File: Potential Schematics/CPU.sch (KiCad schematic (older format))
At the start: 0 parts

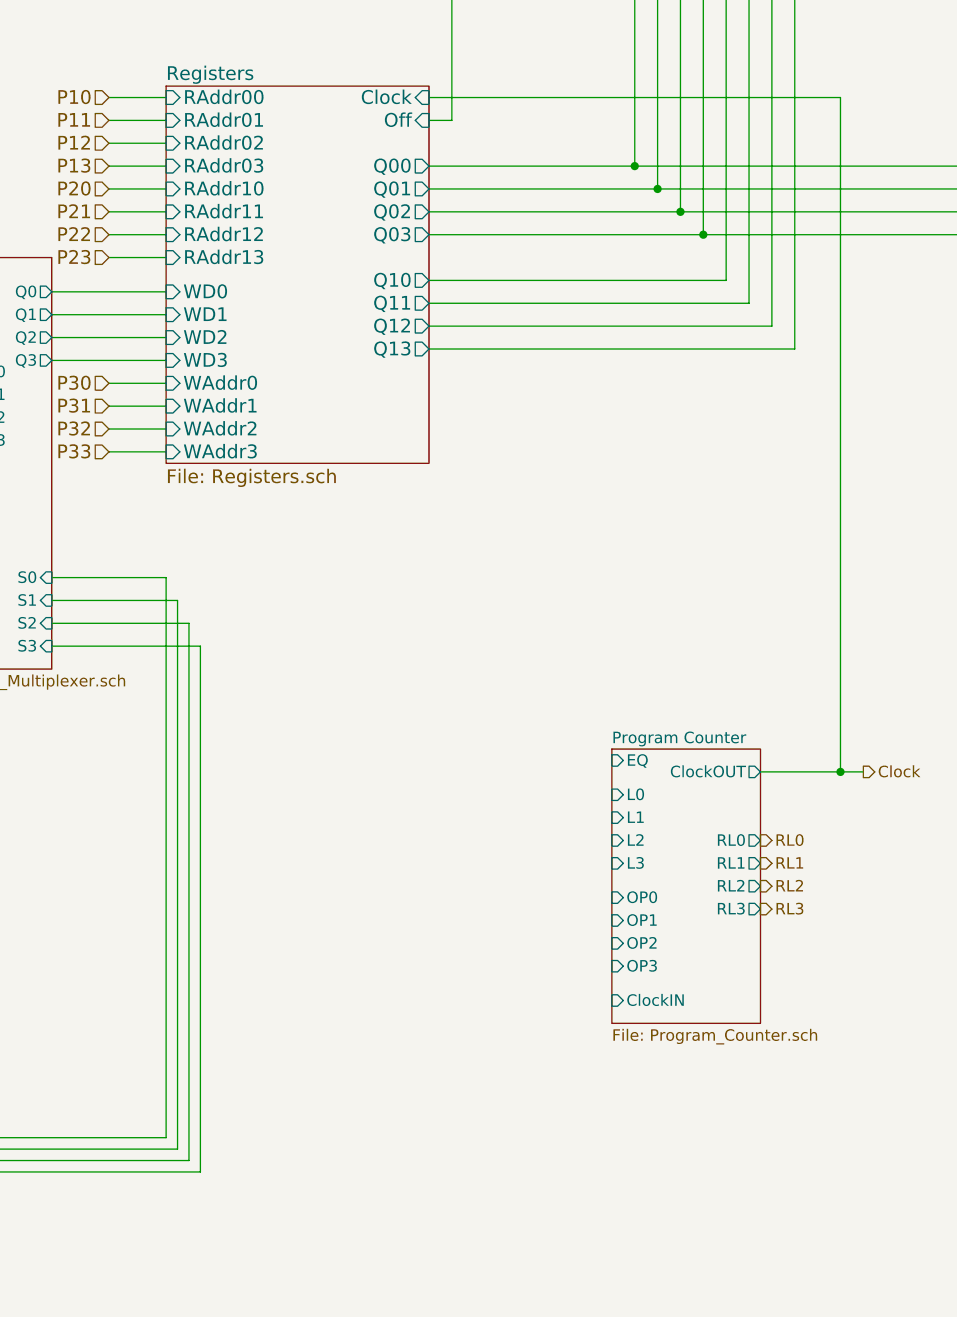
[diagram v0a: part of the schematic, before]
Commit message: In the middle of adding ROM
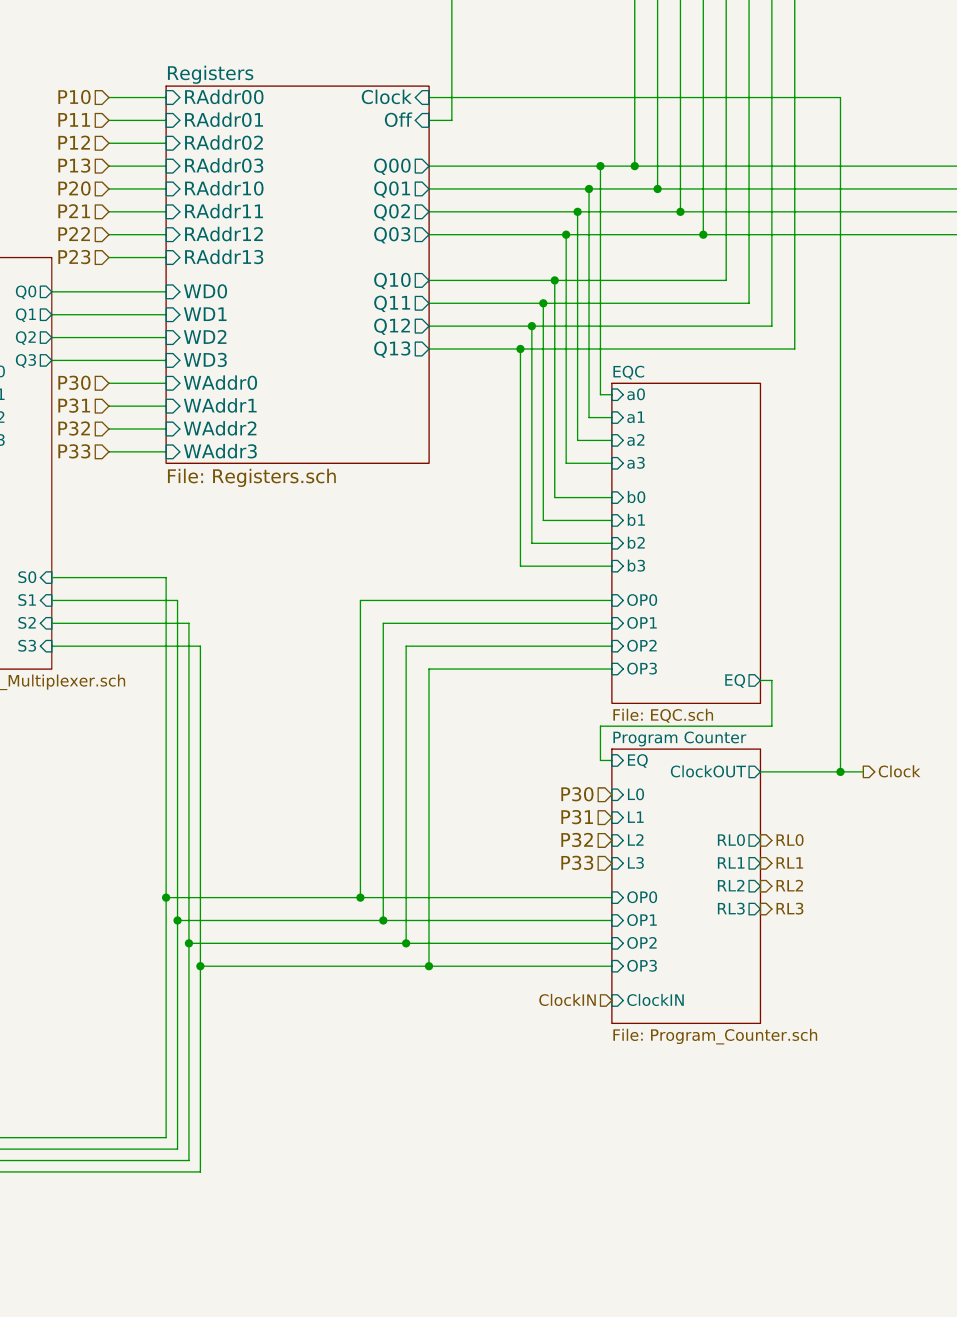
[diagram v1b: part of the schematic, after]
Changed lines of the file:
@@
 $Descr A4 11693 8268
 encoding utf-8
-Sheet 2 902
+Sheet 2 1330
 Title "CPU"
 Date "2018-09-14"
@@
 	6200 3650 6450 3650
 Wire Wire Line
-	7600 2400 8500 2400
+	7600 2400 8350 2400
 Wire Wire Line
 	8500 2400 8500 1650
@@
 	2700 2200 2800 2200
 Wire Wire Line
-	7600 2500 8600 2500
+	7600 2500 8300 2500
 Wire Wire Line
 	8600 2500 8600 1550
@@
 	8700 1450 8700 2600
 Wire Wire Line
-	8700 2600 7600 2600
-Wire Wire Line
-	7600 2700 8800 2700
+	8700 2600 8250 2600
+Wire Wire Line
+	7600 2700 8200 2700
 Wire Wire Line
 	8800 2700 8800 1350
@@
 	7700 2200 7600 2200
 Wire Wire Line
-	7600 2900 8900 2900
+	7600 2900 8150 2900
 Wire Wire Line
 	8900 2900 8900 1250
@@
 	9000 1150 9000 3000
 Wire Wire Line
-	9000 3000 7600 3000
-Wire Wire Line
-	7600 3100 9100 3100
+	9000 3000 8100 3000
+Wire Wire Line
+	7600 3100 8050 3100
 Wire Wire Line
 	9100 3100 9100 1050
@@
 	9200 950  9200 3200
 Wire Wire Line
-	9200 3200 7600 3200
+	9200 3200 8000 3200
 $Sheet
 S 2800 4400 1100 1450
@@
 	1750 6650 6450 6650
 Wire Wire Line
-	6450 6650 6450 4200
+	6450 6650 6450 5600
 Wire Wire Line
 	6450 4200 5950 4200
@@
 	5950 4300 6500 4300
 Wire Wire Line
-	6500 4300 6500 6700
+	6500 4300 6500 5700
 Wire Wire Line
 	6500 6700 1600 6700
@@
 	1450 6750 6550 6750
 Wire Wire Line
-	6550 6750 6550 4400
+	6550 6750 6550 5800
 Wire Wire Line
 	6550 4400 5950 4400
@@
 	5950 4500 6600 4500
 Wire Wire Line
-	6600 4500 6600 6800
+	6600 4500 6600 5900
 Wire Wire Line
 	6600 6800 1300 6800
@@
 Wire Wire Line
 	7700 700  7700 2200
+$Sheet
+S 8400 3350 650  1400
+U 5BAD7F19
+F0 "EQC" 50
+F1 "EQC.sch" 50
+F2 "OP0" I L 8400 4300 50
+F3 "OP1" I L 8400 4400 50
+F4 "OP2" I L 8400 4500 50
+F5 "OP3" I L 8400 4600 50
+F6 "b0" I L 8400 3850 50
+F7 "b1" I L 8400 3950 50
+F8 "b2" I L 8400 4050 50
+F9 "b3" I L 8400 4150 50
+F10 "a0" I L 8400 3400 50
+F11 "a1" I L 8400 3500 50
+F12 "a2" I L 8400 3600 50
+F13 "a3" I L 8400 3700 50
+F14 "EQ" O R 9050 4650 50
+$EndSheet
+Wire Wire Line
+	9050 4650 9100 4650
+Wire Wire Line
+	9100 4650 9100 4850
+Wire Wire Line
+	9100 4850 8350 4850
+Wire Wire Line
+	8350 4850 8350 5000
+Wire Wire Line
+	8350 5000 8400 5000
+Wire Wire Line
+	8350 2400 8350 3400
+Wire Wire Line
+	8350 3400 8400 3400
+Connection ~ 8350 2400
+Wire Wire Line
+	8350 2400 8500 2400
+Wire Wire Line
+	8300 2500 8300 3500
+Wire Wire Line
+	8300 3500 8400 3500
+Connection ~ 8300 2500
+Wire Wire Line
+	8300 2500 8600 2500
+Wire Wire Line
+	8250 2600 8250 3600
+Wire Wire Line
+	8250 3600 8400 3600
+Connection ~ 8250 2600
+Wire Wire Line
+	8250 2600 7600 2600
+Wire Wire Line
+	8200 3700 8400 3700
+Wire Wire Line
+	8200 2700 8200 3700
+Connection ~ 8200 2700
+Wire Wire Line
+	8200 2700 8800 2700
+Wire Wire Line
+	8150 2900 8150 3850
+Wire Wire Line
+	8150 3850 8400 3850
+Connection ~ 8150 2900
+Wire Wire Line
+	8150 2900 8900 2900
+Wire Wire Line
+	8100 3000 8100 3950
+Wire Wire Line
+	8100 3950 8400 3950
+Connection ~ 8100 3000
+Wire Wire Line
+	8100 3000 7600 3000
+Wire Wire Line
+	8050 3100 8050 4050
+Wire Wire Line
+	8050 4050 8400 4050
+Connection ~ 8050 3100
+Wire Wire Line
+	8050 3100 9100 3100
+Wire Wire Line
+	8000 3200 8000 4150
+Wire Wire Line
+	8000 4150 8400 4150
+Connection ~ 8000 3200
+Wire Wire Line
+	8000 3200 7600 3200
+Wire Wire Line
+	8400 5600 7300 5600
+Connection ~ 6450 5600
+Wire Wire Line
+	6450 5600 6450 4200
+Wire Wire Line
+	8400 5700 7400 5700
+Connection ~ 6500 5700
+Wire Wire Line
+	6500 5700 6500 6700
+Wire Wire Line
+	8400 5800 7500 5800
+Connection ~ 6550 5800
+Wire Wire Line
+	6550 5800 6550 4400
+Wire Wire Line
+	8400 5900 7600 5900
+Connection ~ 6600 5900
+Wire Wire Line
+	6600 5900 6600 6800
+Text HLabel 8400 6050 0    50   Input ~ 0
+ClockIN
+Text HLabel 8400 5150 0    60   Input ~ 0
+P30
+Text HLabel 8400 5250 0    60   Input ~ 0
+P31
+Text HLabel 8400 5350 0    60   Input ~ 0
+P32
+Text HLabel 8400 5450 0    60   Input ~ 0
+P33
+Wire Wire Line
+	7300 5600 7300 4300
+Wire Wire Line
+	7300 4300 8400 4300
+Connection ~ 7300 5600
+Wire Wire Line
+	7300 5600 6450 5600
+Wire Wire Line
+	7400 5700 7400 4400
+Wire Wire Line
+	7400 4400 8400 4400
+Connection ~ 7400 5700
+Wire Wire Line
+	7400 5700 6500 5700
+Wire Wire Line
+	7500 5800 7500 4500
+Wire Wire Line
+	7500 4500 8400 4500
+Connection ~ 7500 5800
+Wire Wire Line
+	7500 5800 6550 5800
+Wire Wire Line
+	7600 5900 7600 4600
+Wire Wire Line
+	7600 4600 8400 4600
+Connection ~ 7600 5900
+Wire Wire Line
+	7600 5900 6600 5900
 $EndSCHEMATC
